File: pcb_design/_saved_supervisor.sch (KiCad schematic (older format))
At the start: 20 parts, among them U5 7400-TSSOP, U6 SN74ALVC08PWR, U7 SN74ALVC08PWR, U8 SN74AUP1G74

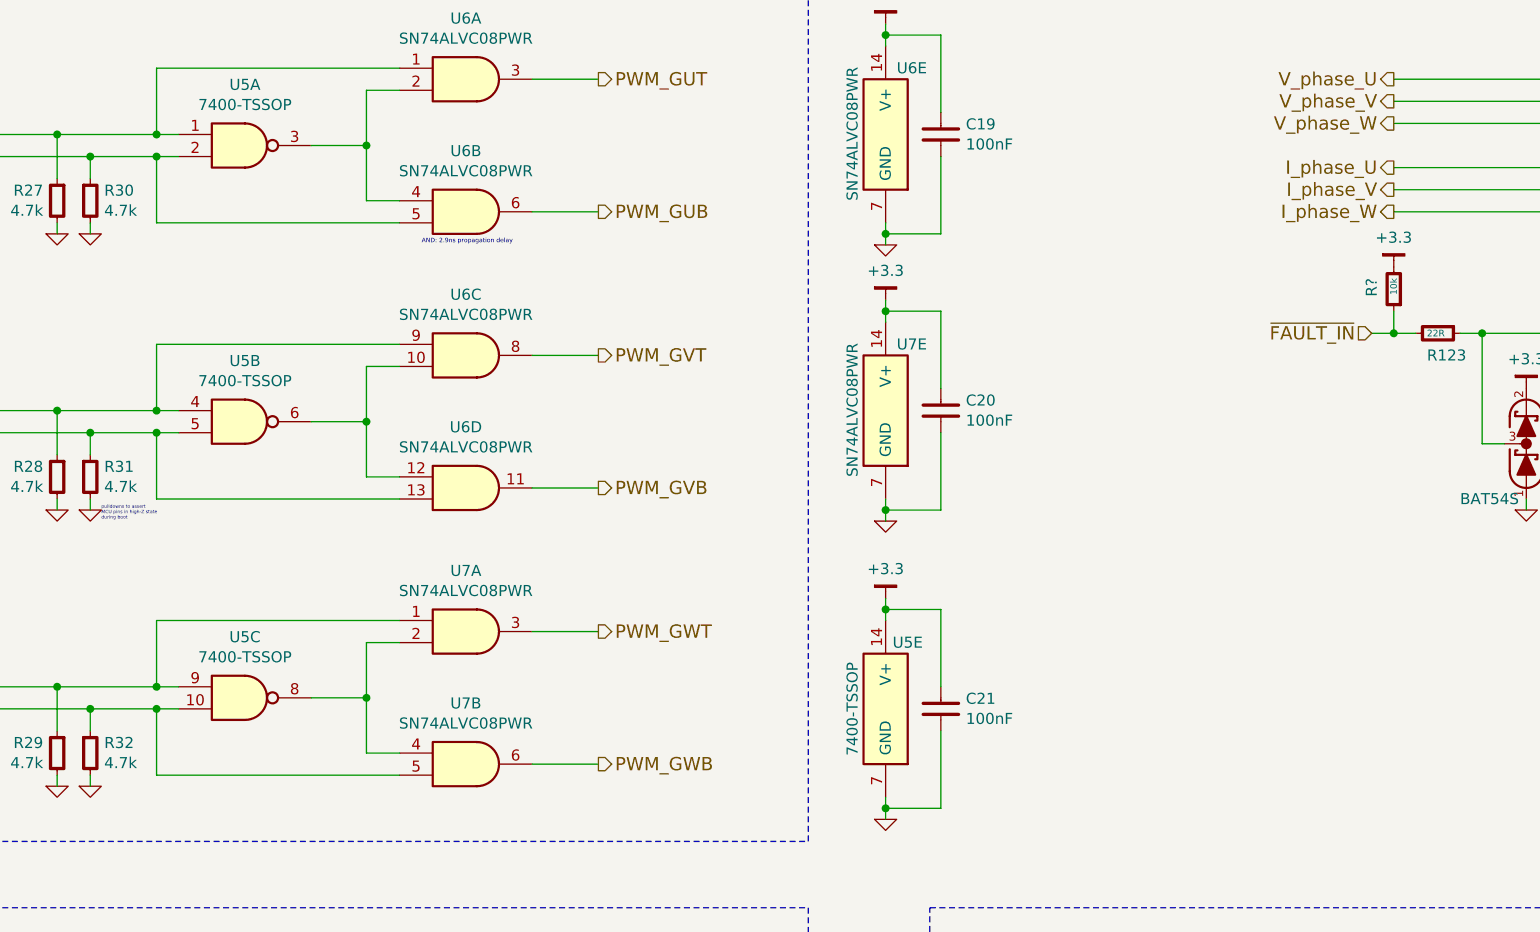
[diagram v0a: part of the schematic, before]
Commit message: Had a missing pullup for the fault signal. Added silkcreens on the bottom
Signed-off-by: Marcos Chaparro <mchaparro@paltatech.com>
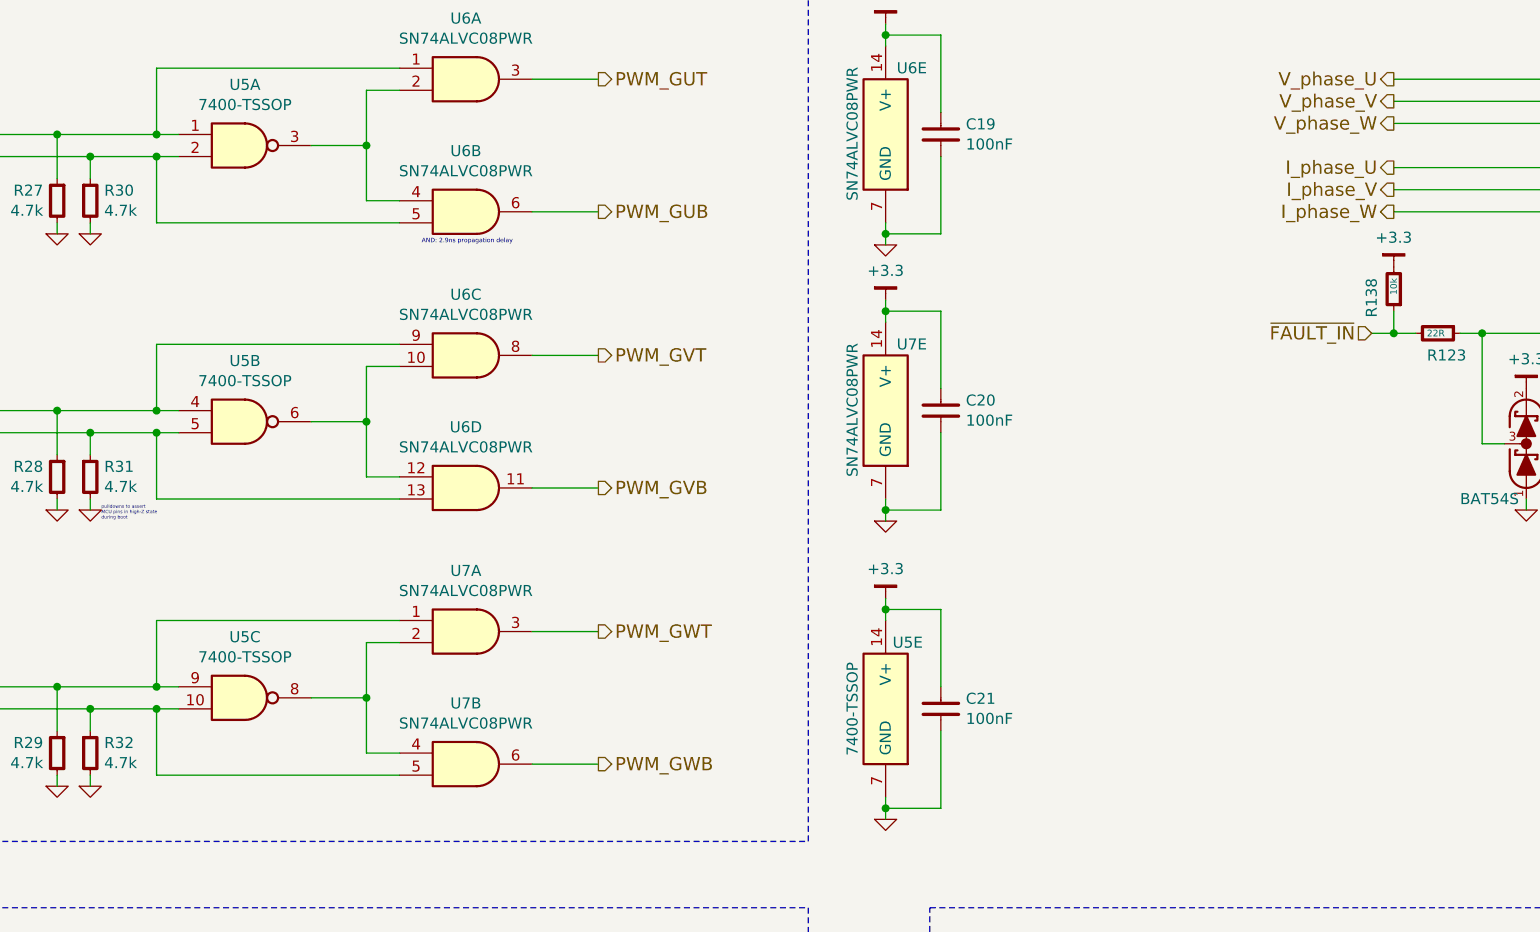
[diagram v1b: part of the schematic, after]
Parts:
- gave numbers to parts that had none: 1
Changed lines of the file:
@@
 	3400 2350 2300 2350
 Wire Wire Line
-	2300 2050 2300 2350
+	2300 2350 2300 2050
 Wire Wire Line
 	1550 2050 2400 2050
@@
 	3400 3600 2300 3600
 Wire Wire Line
-	2300 3300 2300 3600
+	2300 3600 2300 3300
 Wire Wire Line
 	1550 3300 2400 3300
@@
 	3400 4850 2300 4850
 Wire Wire Line
-	2300 4550 2300 4850
+	2300 4850 2300 4550
 Wire Wire Line
 	1550 4550 2400 4550
@@
 Should I protect every output?\nThey are all exposed to ESD \nand a latchup event
 $Comp
-L R-0603 R?
+L R-0603 R138
 U 1 1 589403B1
 P 7900 2650
-F 0 "R?" V 8000 2600 50  0000 L CNN
+F 0 "R138" V 8000 2600 50  0000 L CNN
 F 1 "10k" V 7900 2600 30  0000 L CNN
 F 2 "IPC7351-Nominal:RESC1608X50" H 7900 2650 50  0001 C CNN
@@
 AR Path="/588C2790/589406F0" Ref="#PWR?"  Part="1"
 AR Path="/588C4E84/589406F0" Ref="#PWR?"  Part="1"
-AR Path="/5888D059/589406F0" Ref="#PWR?"  Part="1"
-F 0 "#PWR?" H 7950 2600 30  0001 C CNN
+AR Path="/5888D059/589406F0" Ref="#PWR0125"  Part="1"
+F 0 "#PWR0125" H 7950 2600 30  0001 C CNN
 F 1 "+3.3" H 7900 2683 50  0000 C CNN
 F 2 "" H 50  -2550 60  0000 C CNN
